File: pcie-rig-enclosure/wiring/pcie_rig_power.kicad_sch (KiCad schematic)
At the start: 8 parts, among them J1 12V IN + (red 4 mm binding po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, J2 12V IN - (black 4 mm binding 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, J3 PROBE GND (4 mm binding post,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, J4 Amangny pigtail 3x yellow +12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, M1 Peacefair PZEM-031 DC 8-100 V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, SW1 Ampper 20 A rocker A=supply+ 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

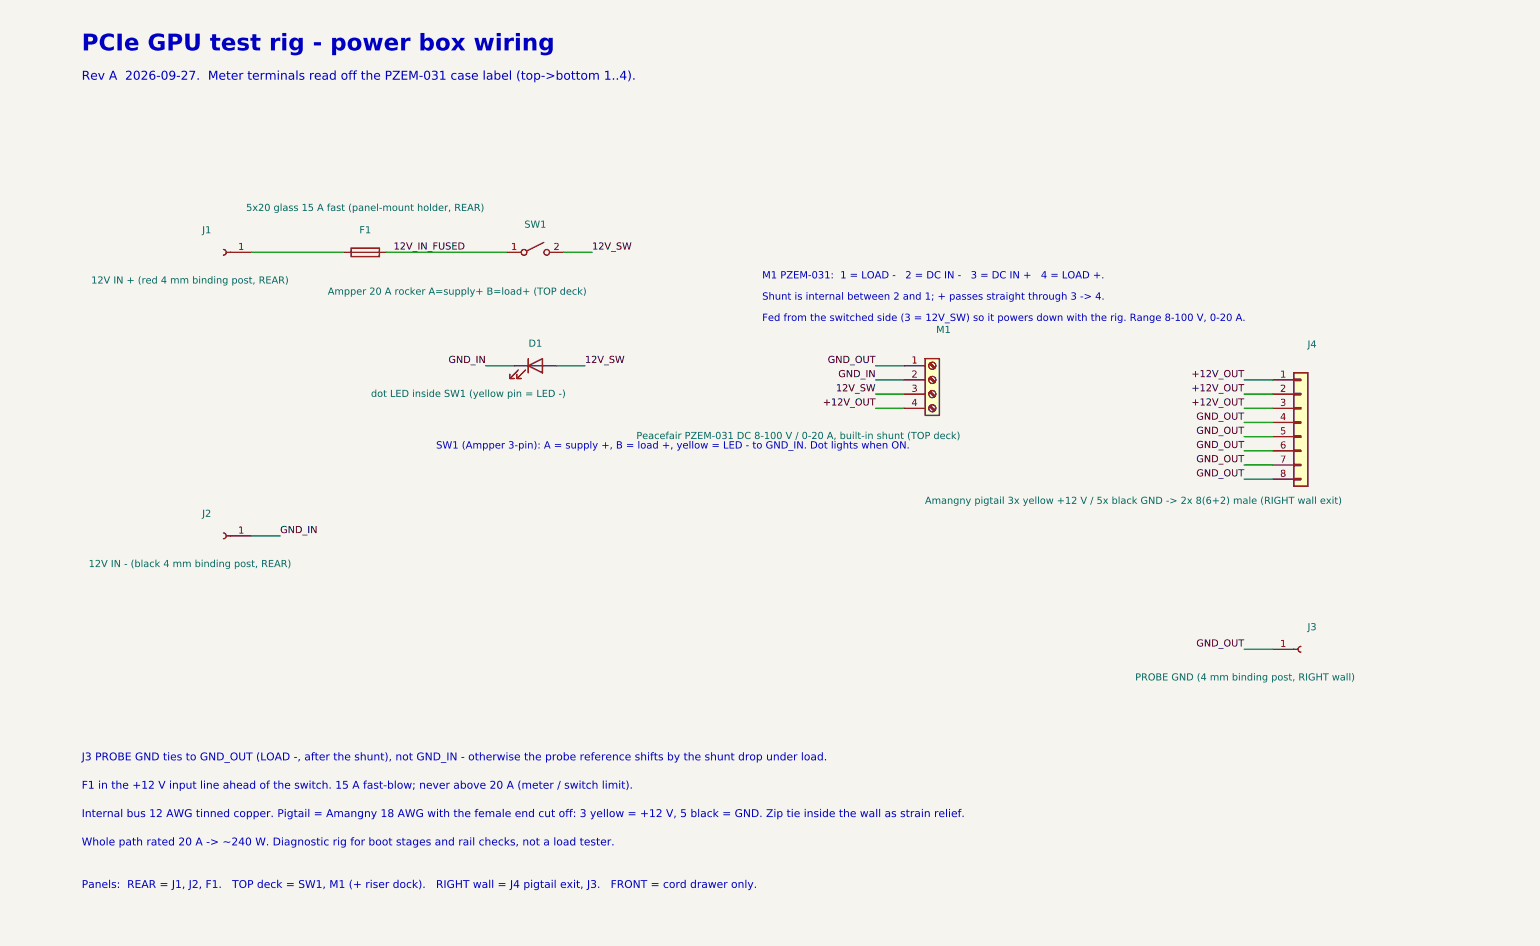
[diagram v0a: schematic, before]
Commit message: docs(pcie-rig-enclosure): redraw schematic with routed wires (rev B), probe post on the top deck, add WIRING.md build guide
Signed-off-by: Aaron Cupp <mrcupp@mrcupp.com>
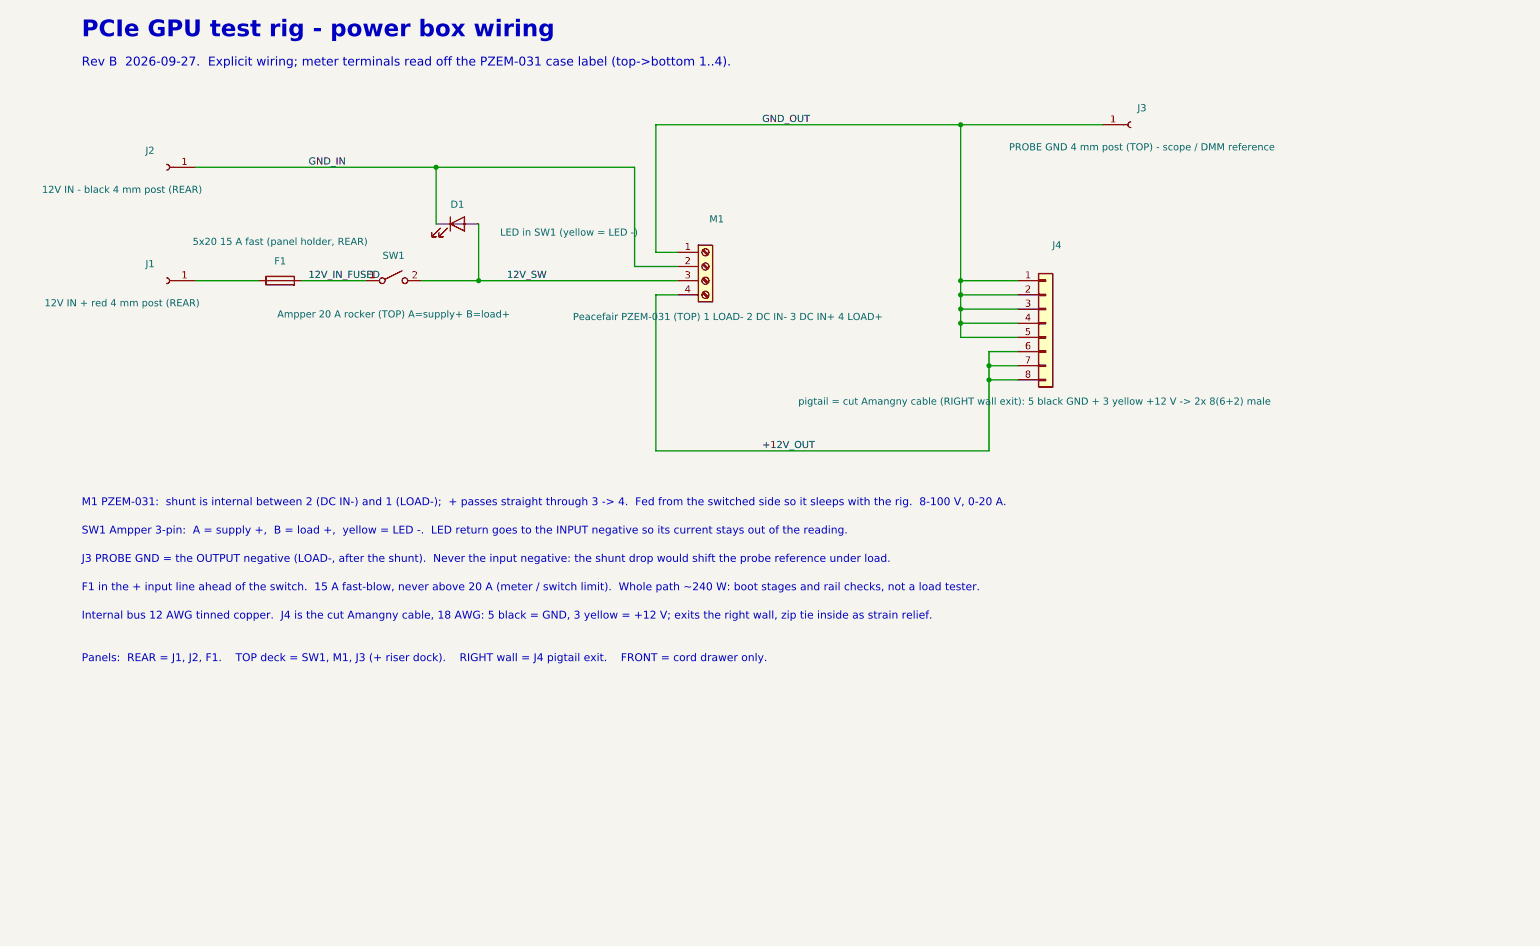
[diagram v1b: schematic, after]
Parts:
- removed F1: 5x20 glass 15 A fast (panel-mount holder, REAR), symbol Device:Fuse
- added J2: 12V IN - black 4 mm post (REAR), symbol Connector:Conn_01x01_Socket
- D1: value dot LED inside SW1 (yellow pin = LED -) -> LED in SW1 (yellow = LED -)
- F1: renamed from J2; value 12V IN - (black 4 mm binding post, REAR) -> 5x20 15 A fast (panel holder, REAR); symbol Connector:Conn_01x01_Socket -> Device:Fuse
- J1: value 12V IN + (red 4 mm binding post, REAR) -> 12V IN + red 4 mm post (REAR)
- J3: value PROBE GND (4 mm binding post, RIGHT wall) -> PROBE GND 4 mm post (TOP) - scope / DMM reference
- J4: value Amangny pigtail 3x yellow +12 V / 5x black GND -> 2x 8(6+2) male (RIGHT wall exit) -> pigtail = cut Amangny cable (RIGHT wall exit): 5 black GND + 3 yellow +12 V -> 2x 8(6+2) male
- M1: value Peacefair PZEM-031 DC 8-100 V / 0-20 A, built-in shunt (TOP deck) -> Peacefair PZEM-031 (TOP) 1 LOAD- 2 DC IN- 3 DC IN+ 4 LOAD+
- SW1: value Ampper 20 A rocker A=supply+ B=load+ (TOP deck) -> Ampper 20 A rocker (TOP) A=supply+ B=load+
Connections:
- net +12V_OUT: now also J4.6 (Pin_6), J4.7 (Pin_7), J4.8 (Pin_8); no longer J4.1 (Pin_1), J4.2 (Pin_2), J4.3 (Pin_3)
- net 12V_IN_FUSED: now also F1.2
- net GND_IN: now also J2.1 (Pin_1); no longer F1.1 (Pin_1)
- net GND_OUT: now also J4.1 (Pin_1), J4.2 (Pin_2), J4.3 (Pin_3); no longer J4.6 (Pin_6), J4.7 (Pin_7), J4.8 (Pin_8)
- net at J1.1 (Pin_1): now also F1.1
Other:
- note added: "F1 in the + input line ahead of the switch. 15 A fast-blow, never above 20 A (meter / switch limit). Whole path ~240 W: boot stages and rail checks, not a load tester."
- note added: "Internal bus 12 AWG tinned copper. J4 is the cut Amangny cable, 18 AWG: 5 black = GND, 3 yellow = +12 V; exits the right wall, zip tie inside as strain relief."
- note added: "J3 PROBE GND = the OUTPUT negative (LOAD-, after the shunt). Never the input negative: the shunt drop would shift the probe reference under load."
- note added: "M1 PZEM-031: shunt is internal between 2 (DC IN-) and 1 (LOAD-); + passes straight through 3 -> 4. Fed from the switched side so it sleeps with the rig. 8-100 V, 0-20 A."
- note added: "Panels: REAR = J1, J2, F1. TOP deck = SW1, M1, J3 (+ riser dock). RIGHT wall = J4 pigtail exit. FRONT = cord drawer only."
- note added: "Rev B 2026-09-27. Explicit wiring; meter terminals read off the PZEM-031 case label (top->bottom 1..4)."
- note added: "SW1 Ampper 3-pin: A = supply +, B = load +, yellow = LED -. LED return goes to the INPUT negative so its current stays out of the reading."
- note removed: "F1 in the +12 V input line ahead of the switch. 15 A fast-blow; never above 20 A (meter / switch limit)."
- note removed: "Fed from the switched side (3 = 12V_SW) so it powers down with the rig. Range 8-100 V, 0-20 A."
- note removed: "Internal bus 12 AWG tinned copper. Pigtail = Amangny 18 AWG with the female end cut off: 3 yellow = +12 V, 5 black = GND. Zip tie inside the wall as strain relief."
- note removed: "J3 PROBE GND ties to GND_OUT (LOAD -, after the shunt), not GND_IN - otherwise the probe reference shifts by the shunt drop under load."
- note removed: "M1 PZEM-031: 1 = LOAD - 2 = DC IN - 3 = DC IN + 4 = LOAD +."
- note removed: "Panels: REAR = J1, J2, F1. TOP deck = SW1, M1 (+ riser dock). RIGHT wall = J4 pigtail exit, J3. FRONT = cord drawer only."
- note removed: "Rev A 2026-09-27. Meter terminals read off the PZEM-031 case label (top->bottom 1..4)."
- note removed: "SW1 (Ampper 3-pin): A = supply +, B = load +, yellow = LED - to GND_IN. Dot lights when ON."
- note removed: "Shunt is internal between 2 and 1; + passes straight through 3 -> 4."
- note removed: "Whole path rated 20 A -> ~240 W. Diagnostic rig for boot stages and rail checks, not a load tester."
- moved on the sheet: F1, J1

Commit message: feat(pcie-rig-enclosure): rev C — XT60 in/out (cutouts gated on measurement), banana pairs both walls, meter ahead of switch, WAGO ground bus, engraved labels; blade fuse inline, pigtail dropped
Signed-off-by: Aaron Cupp <mrcupp@mrcupp.com>
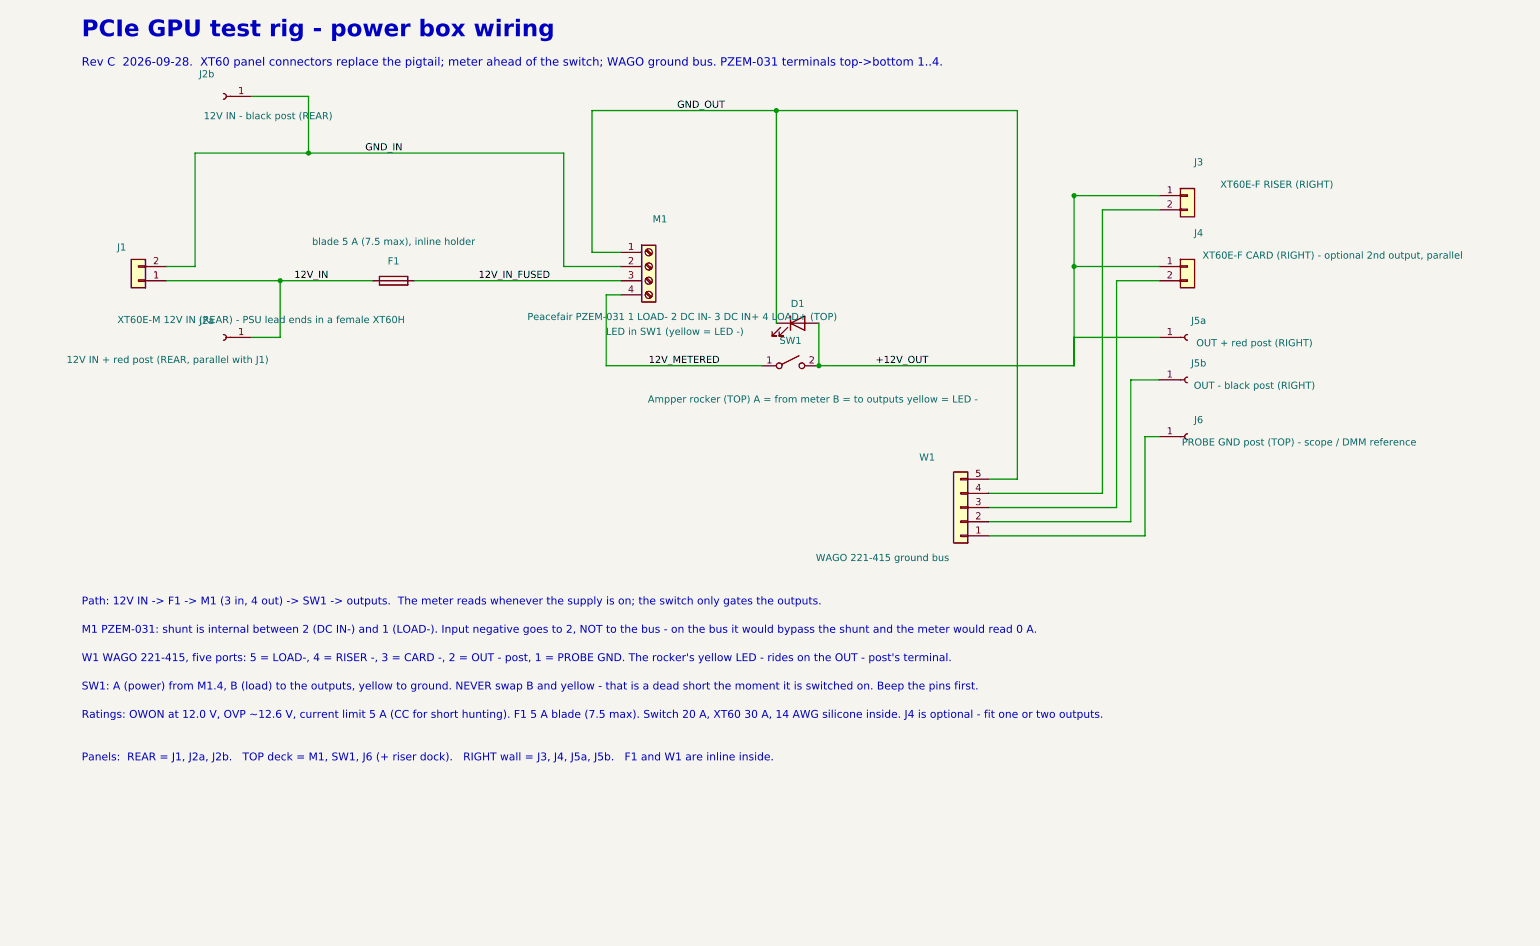
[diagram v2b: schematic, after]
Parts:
- removed J1: 12V IN + red 4 mm post (REAR), symbol Connector:Conn_01x01_Socket
- removed J2: 12V IN - black 4 mm post (REAR), symbol Connector:Conn_01x01_Socket
- removed J3: PROBE GND 4 mm post (TOP) - scope / DMM reference, symbol Connector:Conn_01x01_Socket
- added J2a: 12V IN + red post (REAR, parallel with J1), symbol Connector:Conn_01x01_Socket
- added J3: XT60E-F RISER (RIGHT), symbol Connector_Generic:Conn_01x02
- added J4: XT60E-F CARD (RIGHT) - optional 2nd output, paral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, symbol Connector_Generic:Conn_01x02
- added J5a: OUT + red post (RIGHT), symbol Connector:Conn_01x01_Socket
- added J5b: OUT - black post (RIGHT), symbol Connector:Conn_01x01_Socket
- added J6: PROBE GND post (TOP) - scope / DMM reference, symbol Connector:Conn_01x01_Socket
- added M1: Peacefair PZEM-031 1 LOAD- 2 DC IN- 3 DC IN+ 4 LO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, symbol Connector:Screw_Terminal_01x04
- added W1: WAGO 221-415 ground bus, symbol Connector_Generic:Conn_01x05
- F1: value 5x20 15 A fast (panel holder, REAR) -> blade 5 A (7.5 max), inline holder
- J1: renamed from M1; value Peacefair PZEM-031 (TOP) 1 LOAD- 2 DC IN- 3 DC IN+ 4 LOAD+ -> XT60E-M 12V IN (REAR) - PSU lead ends in a female XT60H; symbol Connector:Screw_Terminal_01x04 -> Connector_Generic:Conn_01x02
- J2b: renamed from J4; value pigtail = cut Amangny cable (RIGHT wall exit): 5 black GND + 3 yellow +12 V -> 2x 8(6+2) male -> 12V IN - black post (REAR); symbol Connector_Generic:Conn_01x08 -> Connector:Conn_01x01_Socket
- SW1: value Ampper 20 A rocker (TOP) A=supply+ B=load+ -> Ampper rocker (TOP) A = from meter B = to outputs yellow = LED -
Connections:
- net +12V_OUT: now also D1.2 (A), SW1.2 (B), J3.1 (Pin_1), J4.1 (Pin_1), J5a.1 (Pin_1); no longer J1.4 (Pin_4), J2b.6 (Pin_6), J2b.7 (Pin_7), J2b.8 (Pin_8)
- net 12V_IN_FUSED: now also M1.3 (Pin_3); no longer SW1.1 (A)
- net GND_IN: now also J2b.1 (Pin_1), M1.2 (Pin_2); no longer D1.1 (K)
- net GND_OUT: now also D1.1 (K), M1.1 (Pin_1), W1.5 (Pin_5); no longer J1.1 (Pin_1), J2b.1 (Pin_1), J2b.2 (Pin_2), J2b.3 (Pin_3), J2b.4 (Pin_4), J2b.5 (Pin_5)
- net 12V_IN: now reaches F1.1
- net 12V_IN: now also J1.1 (Pin_1), J2a.1 (Pin_1)
- removed net 12V_SW: D1.2 (A), J1.3 (Pin_3), SW1.2 (B)
- new net: J6.1 (Pin_1), W1.1 (Pin_1)
- new net: J5b.1 (Pin_1), W1.2 (Pin_2)
- new net: J4.2 (Pin_2), W1.3 (Pin_3)
- new net: J3.2 (Pin_2), W1.4 (Pin_4)
- new net 12V_METERED: M1.4 (Pin_4), SW1.1 (A)
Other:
- note added: "M1 PZEM-031: shunt is internal between 2 (DC IN-) and 1 (LOAD-). Input negative goes to 2, NOT to the bus - on the bus it would bypass the shunt and the meter would read 0 A."
- note added: "Panels: REAR = J1, J2a, J2b. TOP deck = M1, SW1, J6 (+ riser dock). RIGHT wall = J3, J4, J5a, J5b. F1 and W1 are inline inside."
- note added: "Path: 12V IN -> F1 -> M1 (3 in, 4 out) -> SW1 -> outputs. The meter reads whenever the supply is on; the switch only gates the outputs."
- note added: "Ratings: OWON at 12.0 V, OVP ~12.6 V, current limit 5 A (CC for short hunting). F1 5 A blade (7.5 max). Switch 20 A, XT60 30 A, 14 AWG silicone inside. J4 is optional - fit one or two outputs."
- note added: "Rev C 2026-09-28. XT60 panel connectors replace the pigtail; meter ahead of the switch; WAGO ground bus. PZEM-031 terminals top->bottom 1..4."
- note added: "SW1: A (power) from M1.4, B (load) to the outputs, yellow to ground. NEVER swap B and yellow - that is a dead short the moment it is switched on. Beep the pins first."
- note added: "W1 WAGO 221-415, five ports: 5 = LOAD-, 4 = RISER -, 3 = CARD -, 2 = OUT - post, 1 = PROBE GND. The rocker's yellow LED - rides on the OUT - post's terminal."
- note removed: "F1 in the + input line ahead of the switch. 15 A fast-blow, never above 20 A (meter / switch limit). Whole path ~240 W: boot stages and rail checks, not a load tester."
- note removed: "Internal bus 12 AWG tinned copper. J4 is the cut Amangny cable, 18 AWG: 5 black = GND, 3 yellow = +12 V; exits the right wall, zip tie inside as strain relief."
- note removed: "J3 PROBE GND = the OUTPUT negative (LOAD-, after the shunt). Never the input negative: the shunt drop would shift the probe reference under load."
- note removed: "M1 PZEM-031: shunt is internal between 2 (DC IN-) and 1 (LOAD-); + passes straight through 3 -> 4. Fed from the switched side so it sleeps with the rig. 8-100 V, 0-20 A."
- note removed: "Panels: REAR = J1, J2, F1. TOP deck = SW1, M1, J3 (+ riser dock). RIGHT wall = J4 pigtail exit. FRONT = cord drawer only."
- note removed: "Rev B 2026-09-27. Explicit wiring; meter terminals read off the PZEM-031 case label (top->bottom 1..4)."
- note removed: "SW1 Ampper 3-pin: A = supply +, B = load +, yellow = LED -. LED return goes to the INPUT negative so its current stays out of the reading."
